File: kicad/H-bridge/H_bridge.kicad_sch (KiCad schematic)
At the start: 40 parts, among them J1 Screw_Terminal_01x03, J2 Conn_Coaxial, J3 2453710000, J4 Screw_Terminal_01x02, Q1 IAUT300N10S5N014ATMA1, Q2 IAUT300N10S5N014ATMA1, Q3 IAUT300N10S5N014ATMA1, Q4 IAUT300N10S5N014ATMA1, U1 LTV-817, U2 PDS1-S15-S15-M, U3 HIP4080A

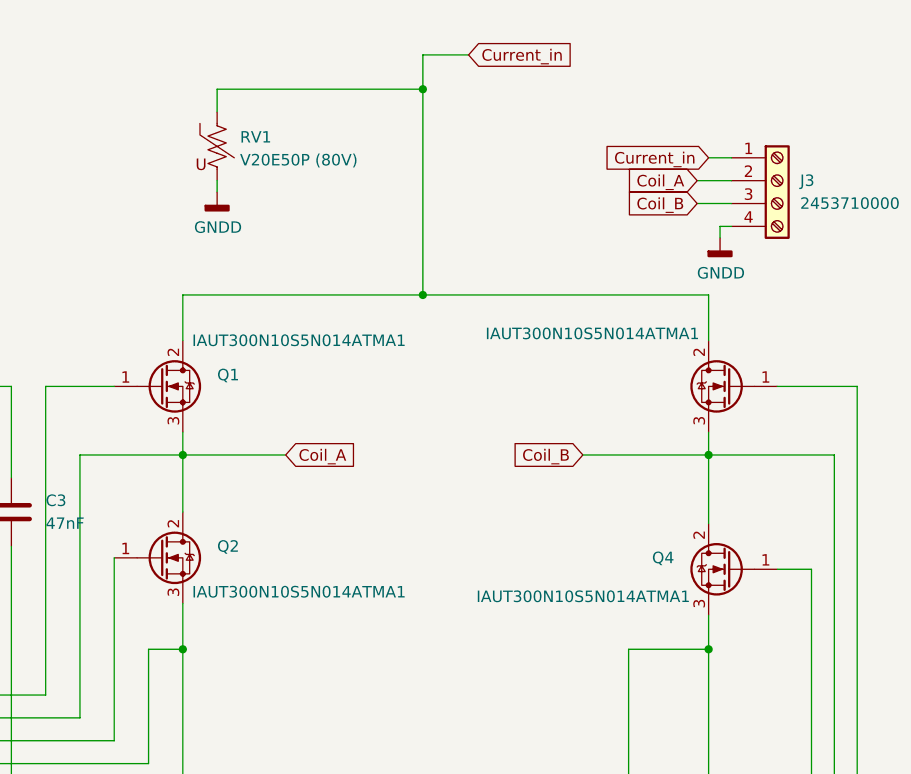
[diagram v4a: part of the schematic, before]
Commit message: Fixed error is MOS package assigment and added solder mask for manual tin pour for increased conductivity
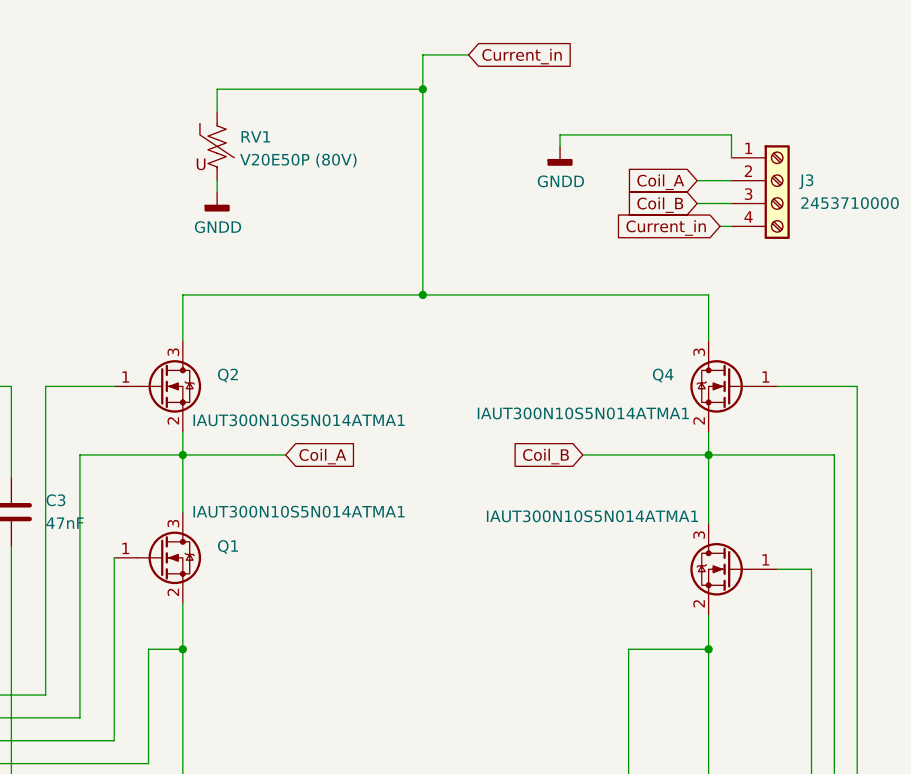
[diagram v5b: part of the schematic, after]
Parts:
- Q1, Q2, Q3, Q4: symbol Device:Q_NMOS_GDS -> Device:Q_NMOS_GSD
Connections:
- net Current_in: now also J3.4 (Pin_4), Q2.3 (D), Q4.3 (D); no longer J3.1 (Pin_1), Q1.2 (D), Q3.2 (D)
- net GNDD: now also J3.1 (Pin_1), Q1.2 (S), Q3.2 (S); no longer J3.4 (Pin_4), Q2.3 (S), Q4.3 (S)
- net at Q4.1 (G): now also U3.11 (AHO); no longer U3.13 (ALO)
- net at Q3.1 (G): now also U3.13 (ALO); no longer U3.11 (AHO)
- net at Q1.1 (G): now also U3.18 (BLO); no longer U3.20 (BHO)
- net at Q2.1 (G): now also U3.20 (BHO); no longer U3.18 (BLO)
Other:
- moved on the sheet: Q1, Q2, Q4
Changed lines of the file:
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@@
 	(wire
 		(pts
+			(xy 262.89 44.45) (xy 264.16 44.45)
+		)
+		(stroke
+			(width 0)
+			(type default)
+		)
+	)
+	(wire
+		(pts
 			(xy 160.02 96.52) (xy 187.96 96.52)
 		)
@@
 	(wire
 		(pts
+			(xy 245.11 34.29) (xy 264.16 34.29)
+		)
+		(stroke
+			(width 0)
+			(type default)
+		)
+	)
+	(wire
+		(pts
 			(xy 26.67 95.25) (xy 26.67 92.71)
 		)
@@
 	(wire
 		(pts
-			(xy 261.62 36.83) (xy 264.16 36.83)
-		)
-		(stroke
-			(width 0)
-			(type default)
-		)
-	)
-	(wire
-		(pts
 			(xy 151.13 62.23) (xy 180.34 62.23)
 		)
@@
 	(wire
 		(pts
-			(xy 264.16 44.45) (xy 262.89 44.45)
-		)
-		(stroke
-			(width 0)
-			(type default)
-		)
-	)
-	(wire
-		(pts
 			(xy 106.68 113.03) (xy 106.68 115.57)
 		)
@@
 	(wire
 		(pts
+			(xy 264.16 34.29) (xy 264.16 36.83)
+		)
+		(stroke
+			(width 0)
+			(type default)
+		)
+	)
+	(wire
+		(pts
 			(xy 229.87 25.4) (xy 234.95 25.4)
 		)
@@
 	(wire
 		(pts
-			(xy 262.89 44.45) (xy 262.89 45.72)
+			(xy 245.11 34.29) (xy 245.11 35.56)
 		)
 		(stroke
@@
 	(global_label "Current_in"
 		(shape input)
-		(at 261.62 36.83 180)
+		(at 262.89 44.45 180)
 		(fields_autoplaced yes)
 		(effects
@@
 		)
 		(property "Intersheetrefs" "${INTERSHEET_REFS}"
-			(at 249.6129 36.83 0)
+			(at 250.8829 44.45 0)
 			(effects
 				(font
@@
 	(symbol
 		(lib_id "Coil_speedifier-rescue:GNDD-power")
-		(at 262.89 45.72 0)
+		(at 245.11 35.56 0)
 		(unit 1)
 		(exclude_from_sim no)
@@
 		(dnp no)
 		(property "Reference" "#PWR016"
-			(at 262.89 52.07 0)
+			(at 245.11 41.91 0)
 			(effects
 				(font
@@
 		)
 		(property "Value" "GNDD"
-			(at 262.9916 49.657 0)
+			(at 245.2116 39.497 0)
 			(effects
 				(font
@@
 		)
 		(property "Footprint" ""
-			(at 262.89 45.72 0)
+			(at 245.11 35.56 0)
 			(effects
 				(font
@@
 		)
 		(property "Datasheet" ""
-			(at 262.89 45.72 0)
+			(at 245.11 35.56 0)
 			(effects
 				(font
@@
 		)
 		(property "Description" ""
-			(at 262.89 45.72 0)
+			(at 245.11 35.56 0)
 			(effects
 				(font
@@
 	)
 	(symbol
-		(lib_id "Device:Q_NMOS_GDS")
-		(at 264.16 82.55 0)
+		(lib_id "Device:Q_NMOS_GSD")
+		(at 264.16 62.23 0)
 		(mirror y)
 		(unit 1)
@@
 		(dnp no)
 		(property "Reference" "Q4"
-			(at 257.81 81.2799 0)
+			(at 257.81 60.9599 0)
 			(effects
 				(font
@@
 		)
 		(property "Value" "IAUT300N10S5N014ATMA1"
-			(at 259.588 85.598 0)
+			(at 259.588 65.278 0)
 			(effects
 				(font
@@
 		)
 		(property "Footprint" "Package_TO_SOT_SMD:Infineon_PG-HSOF-8-1_ThermalVias"
-			(at 259.08 80.01 0)
+			(at 259.08 59.69 0)
 			(effects
 				(font
@@
 			)
 		)
-		(property "Datasheet" "https://ngspice.sourceforge.io/docs/ngspice-html-manual/manual.xhtml#cha_MOSFETs"
-			(at 264.16 95.25 0)
+		(property "Datasheet" "~"
+			(at 264.16 62.23 0)
 			(effects
 				(font
@@
 			)
 		)
-		(property "Description" "N-MOSFET transistor, drain/source/gate"
-			(at 264.16 82.55 0)
+		(property "Description" "N-MOSFET transistor, gate/source/drain"
+			(at 264.16 62.23 0)
 			(effects
 				(font
@@
 		)
 		(property "Sim.Device" "NMOS"
-			(at 264.16 99.695 0)
+			(at 264.16 79.375 0)
 			(effects
 				(font
@@
 		)
 		(property "Sim.Type" "VDMOS"
-			(at 264.16 101.6 0)
+			(at 264.16 81.28 0)
 			(effects
 				(font
@@
 		)
 		(property "Sim.Pins" "1=D 2=G 3=S"
-			(at 264.16 97.79 0)
+			(at 264.16 77.47 0)
 			(effects
 				(font
@@
 		)
 		(property "PARTNO" "IAUT300N10S5N014ATMA1"
-			(at 264.16 82.55 0)
+			(at 264.16 62.23 0)
 			(effects
 				(font
@@
 		)
 		(property "DIGIKEY" "448-IAUT300N10S5N014ATMA1CT-ND"
-			(at 264.16 82.55 0)
+			(at 264.16 62.23 0)
 			(effects
 				(font
@@
 		(exclude_from_sim yes)
 		(in_bom yes)
-		(on_board yes)
+		(on_board no)
 		(dnp no)
 		(property "Reference" "BOM1"
@@
 	)
 	(symbol
-		(lib_id "Device:Q_NMOS_GDS")
-		(at 264.16 62.23 0)
+		(lib_id "Device:Q_NMOS_GSD")
+		(at 264.16 82.55 0)
 		(mirror y)
 		(unit 1)
@@
 		(dnp no)
 		(property "Reference" "Q3"
-			(at 257.81 60.9599 0)
+			(at 257.81 81.2799 0)
 			(effects
 				(font
@@
 		)
 		(property "Value" "IAUT300N10S5N014ATMA1"
-			(at 260.604 56.388 0)
+			(at 260.604 76.708 0)
 			(effects
 				(font
@@
 		)
 		(property "Footprint" "Package_TO_SOT_SMD:Infineon_PG-HSOF-8-1_ThermalVias"
-			(at 259.08 59.69 0)
+			(at 259.08 80.01 0)
 			(effects
 				(font
@@
 			)
 		)
-		(property "Datasheet" "https://ngspice.sourceforge.io/docs/ngspice-html-manual/manual.xhtml#cha_MOSFETs"
-			(at 264.16 74.93 0)
+		(property "Datasheet" "~"
+			(at 264.16 82.55 0)
 			(effects
 				(font
@@
 			)
 		)
-		(property "Description" "N-MOSFET transistor, drain/source/gate"
-			(at 264.16 62.23 0)
+		(property "Description" "N-MOSFET transistor, gate/source/drain"
+			(at 264.16 82.55 0)
 			(effects
 				(font
@@
 		)
 		(property "Sim.Device" "NMOS"
-			(at 264.16 79.375 0)
+			(at 264.16 99.695 0)
 			(effects
 				(font
@@
 		)
 		(property "Sim.Type" "VDMOS"
-			(at 264.16 81.28 0)
+			(at 264.16 101.6 0)
 			(effects
 				(font
@@
 		)
 		(property "Sim.Pins" "1=D 2=G 3=S"
-			(at 264.16 77.47 0)
+			(at 264.16 97.79 0)
 			(effects
 				(font
@@
 		)
 		(property "PARTNO" "IAUT300N10S5N014ATMA1"
-			(at 264.16 62.23 0)
+			(at 264.16 82.55 0)
 			(effects
 				(font
@@
 		)
 		(property "DIGIKEY" "448-IAUT300N10S5N014ATMA1CT-ND"
-			(at 264.16 62.23 0)
+			(at 264.16 82.55 0)
 			(effects
 				(font
@@
 	)
 	(symbol
-		(lib_id "Device:Q_NMOS_GDS")
-		(at 200.66 62.23 0)
+		(lib_id "Device:Q_NMOS_GSD")
+		(at 200.66 81.28 0)
 		(unit 1)
 		(exclude_from_sim no)
@@
 		(dnp no)
 		(property "Reference" "Q1"
-			(at 207.01 60.9599 0)
+			(at 207.01 80.0099 0)
 			(effects
 				(font
@@
 		)
 		(property "Value" "IAUT300N10S5N014ATMA1"
-			(at 204.216 57.15 0)
+			(at 204.216 76.2 0)
 			(effects
 				(font
@@
 		)
 		(property "Footprint" "Package_TO_SOT_SMD:Infineon_PG-HSOF-8-1_ThermalVias"
-			(at 205.74 59.69 0)
+			(at 205.74 78.74 0)
 			(effects
 				(font
@@
 			)
 		)
-		(property "Datasheet" "https://ngspice.sourceforge.io/docs/ngspice-html-manual/manual.xhtml#cha_MOSFETs"
-			(at 200.66 74.93 0)
+		(property "Datasheet" "~"
+			(at 200.66 81.28 0)
 			(effects
 				(font
@@
 			)
 		)
-		(property "Description" "N-MOSFET transistor, drain/source/gate"
-			(at 200.66 62.23 0)
+		(property "Description" "N-MOSFET transistor, gate/source/drain"
+			(at 200.66 81.28 0)
 			(effects
 				(font
@@
 		)
 		(property "Sim.Device" "NMOS"
-			(at 200.66 79.375 0)
+			(at 200.66 98.425 0)
 			(effects
 				(font
@@
 		)
 		(property "Sim.Type" "VDMOS"
-			(at 200.66 81.28 0)
+			(at 200.66 100.33 0)
 			(effects
 				(font
@@
 		)
 		(property "Sim.Pins" "1=D 2=G 3=S"
-			(at 200.66 77.47 0)
+			(at 200.66 96.52 0)
 			(effects
 				(font
@@
 		)
 		(property "PARTNO" "IAUT300N10S5N014ATMA1"
-			(at 200.66 62.23 0)
+			(at 200.66 81.28 0)
 			(effects
 				(font
@@
 		)
 		(property "DIGIKEY" "448-IAUT300N10S5N014ATMA1CT-ND"
-			(at 200.66 62.23 0)
+			(at 200.66 81.28 0)
 			(effects
 				(font
@@
 	)
 	(symbol
-		(lib_id "Device:Q_NMOS_GDS")
-		(at 200.66 81.28 0)
+		(lib_id "Device:Q_NMOS_GSD")
+		(at 200.66 62.23 0)
 		(unit 1)
 		(exclude_from_sim no)
@@
 		(dnp no)
 		(property "Reference" "Q2"
-			(at 207.01 80.0099 0)
+			(at 207.01 60.9599 0)
 			(effects
 				(font
@@
 		)
 		(property "Value" "IAUT300N10S5N014ATMA1"
-			(at 204.216 85.09 0)
+			(at 204.216 66.04 0)
 			(effects
 				(font
@@
 		)
 		(property "Footprint" "Package_TO_SOT_SMD:Infineon_PG-HSOF-8-1_ThermalVias"
-			(at 205.74 78.74 0)
+			(at 205.74 59.69 0)
 			(effects
 				(font
@@
 			)
 		)
-		(property "Datasheet" "https://ngspice.sourceforge.io/docs/ngspice-html-manual/manual.xhtml#cha_MOSFETs"
-			(at 200.66 93.98 0)
+		(property "Datasheet" "~"
+			(at 200.66 62.23 0)
 			(effects
 				(font
@@
 			)
 		)
-		(property "Description" "N-MOSFET transistor, drain/source/gate"
-			(at 200.66 81.28 0)
+		(property "Description" "N-MOSFET transistor, gate/source/drain"
+			(at 200.66 62.23 0)
 			(effects
 				(font
@@
 		)
 		(property "Sim.Device" "NMOS"
-			(at 200.66 98.425 0)
+			(at 200.66 79.375 0)
 			(effects
 				(font
@@
 		)
 		(property "Sim.Type" "VDMOS"
-			(at 200.66 100.33 0)
+			(at 200.66 81.28 0)
 			(effects
 				(font
@@
 		)
 		(property "Sim.Pins" "1=D 2=G 3=S"
-			(at 200.66 96.52 0)
+			(at 200.66 77.47 0)
 			(effects
 				(font
@@
 		)
 		(property "PARTNO" "IAUT300N10S5N014ATMA1"
-			(at 200.66 81.28 0)
+			(at 200.66 62.23 0)
 			(effects
 				(font
@@
 		)
 		(property "DIGIKEY" "448-IAUT300N10S5N014ATMA1CT-ND"
-			(at 200.66 81.28 0)
+			(at 200.66 62.23 0)
 			(effects
 				(font
